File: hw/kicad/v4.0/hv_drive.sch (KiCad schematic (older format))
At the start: 21 parts, among them P6 CONN_01X02, P8 CONN_01X03, U12 IRAM256a

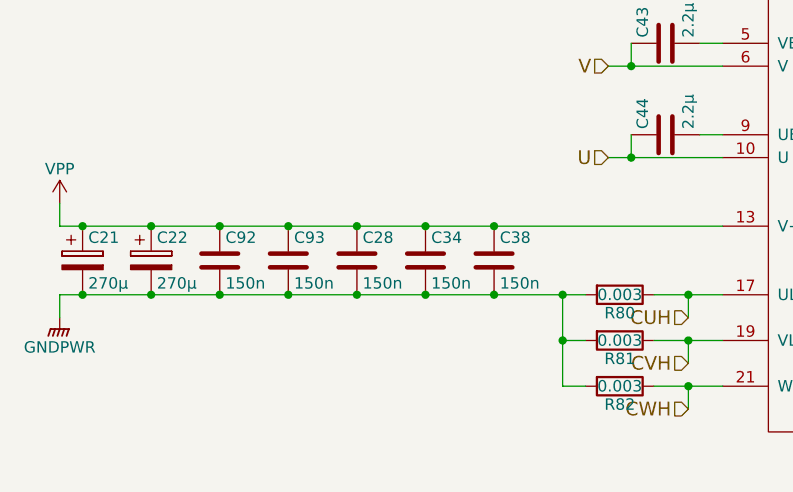
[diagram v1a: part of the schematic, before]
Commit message: Changed 120uf 1808 to 1210 100uF
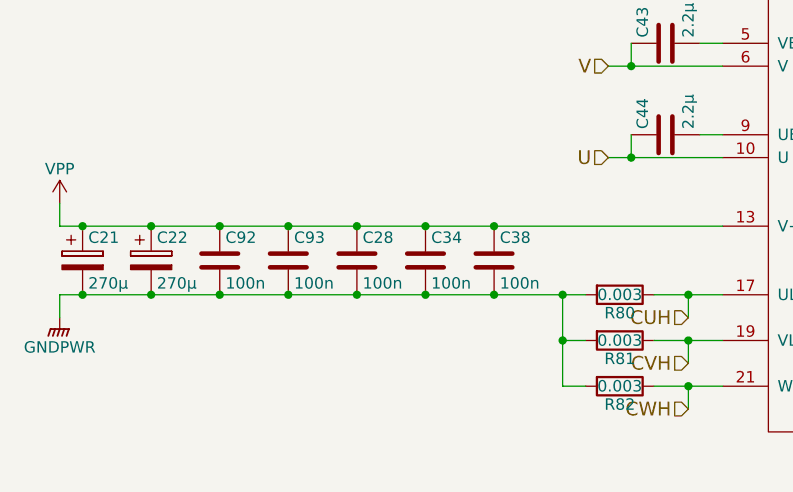
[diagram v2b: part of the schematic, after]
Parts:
- C14: LCSC C15850 -> C15850
- C147, C63: LCSC C14663 -> C14663
- C28, C34, C38, C92, C93: value 150n -> 100n; footprint stmbl:C_1808 -> Capacitor_SMD:C_1210_3225Metric; LCSC (none) -> C141218; Manufacturer No C1808W154KCRACTU -> C1210C104KCRAC7800
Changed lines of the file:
@@
 P 4250 4400
 F 0 "C28" H 4275 4500 50  0000 L CNN
-F 1 "150n" H 4275 4300 50  0000 L CNN
-F 2 "stmbl:C_1808" H 4288 4250 30  0001 C CNN
+F 1 "100n" H 4275 4300 50  0000 L CNN
+F 2 "Capacitor_SMD:C_1210_3225Metric" H 4288 4250 30  0001 C CNN
 F 3 "" H 4250 4400 60  0000 C CNN
 F 4 "" H 4250 4400 60  0001 C CNN "InternalName"
-F 5 "C1808W154KCRACTU" H 4250 4400 60  0001 C CNN "Manufacturer No"
+F 5 "C1210C104KCRAC7800" H 4250 4400 60  0001 C CNN "Manufacturer No"
 F 6 "500V" H 4250 4400 60  0001 C CNN "Voltage"
 F 7 "" H 4250 4400 60  0001 C CNN "Source"
@@
 F 9 "" H 0   0   50  0001 C CNN "Description"
 F 10 "KEMET" H 0   0   50  0001 C CNN "Manufacturer"
+F 11 "C141218" H 4250 4400 50  0001 C CNN "LCSC"
 	1    4250 4400
 	1    0    0    -1
@@
 P 4550 4400
 F 0 "C34" H 4575 4500 50  0000 L CNN
-F 1 "150n" H 4575 4300 50  0000 L CNN
-F 2 "stmbl:C_1808" H 4588 4250 30  0001 C CNN
+F 1 "100n" H 4575 4300 50  0000 L CNN
+F 2 "Capacitor_SMD:C_1210_3225Metric" H 4588 4250 30  0001 C CNN
 F 3 "" H 4550 4400 60  0000 C CNN
 F 4 "" H 4550 4400 60  0001 C CNN "InternalName"
-F 5 "C1808W154KCRACTU" H 4550 4400 60  0001 C CNN "Manufacturer No"
+F 5 "C1210C104KCRAC7800" H 4550 4400 60  0001 C CNN "Manufacturer No"
 F 6 "500V" H 4550 4400 60  0001 C CNN "Voltage"
 F 7 "" H 4550 4400 60  0001 C CNN "Source"
@@
 F 9 "" H 0   0   50  0001 C CNN "Description"
 F 10 "KEMET" H 0   0   50  0001 C CNN "Manufacturer"
+F 11 "C141218" H 4550 4400 50  0001 C CNN "LCSC"
 	1    4550 4400
 	1    0    0    -1
@@
 F 9 "" H 0   0   50  0001 C CNN "Description"
 F 10 "" H 0   0   50  0001 C CNN "Manufacturer"
-F 11 " C14663" H 7800 4900 50  0001 C CNN "LCSC"
+F 11 "C14663" H 7800 4900 50  0001 C CNN "LCSC"
 	1    7800 4900
 	1    0    0    -1
@@
 P 4850 4400
 F 0 "C38" H 4875 4500 50  0000 L CNN
-F 1 "150n" H 4875 4300 50  0000 L CNN
-F 2 "stmbl:C_1808" H 4888 4250 30  0001 C CNN
+F 1 "100n" H 4875 4300 50  0000 L CNN
+F 2 "Capacitor_SMD:C_1210_3225Metric" H 4888 4250 30  0001 C CNN
 F 3 "" H 4850 4400 60  0000 C CNN
 F 4 "" H 4850 4400 60  0001 C CNN "InternalName"
-F 5 "C1808W154KCRACTU" H 4850 4400 60  0001 C CNN "Manufacturer No"
+F 5 "C1210C104KCRAC7800" H 4850 4400 60  0001 C CNN "Manufacturer No"
 F 6 "500V" H 4850 4400 60  0001 C CNN "Voltage"
 F 7 "" H 4850 4400 60  0001 C CNN "Source"
@@
 F 9 "" H 0   0   50  0001 C CNN "Description"
 F 10 "KEMET" H 0   0   50  0001 C CNN "Manufacturer"
+F 11 "C141218" H 4850 4400 50  0001 C CNN "LCSC"
 	1    4850 4400
 	1    0    0    -1
@@
 P 3950 4400
 F 0 "C93" H 3975 4500 50  0000 L CNN
-F 1 "150n" H 3975 4300 50  0000 L CNN
-F 2 "stmbl:C_1808" H 3988 4250 30  0001 C CNN
+F 1 "100n" H 3975 4300 50  0000 L CNN
+F 2 "Capacitor_SMD:C_1210_3225Metric" H 3988 4250 30  0001 C CNN
 F 3 "" H 3950 4400 60  0000 C CNN
 F 4 "" H 3950 4400 60  0001 C CNN "InternalName"
-F 5 "C1808W154KCRACTU" H 3950 4400 60  0001 C CNN "Manufacturer No"
+F 5 "C1210C104KCRAC7800" H 3950 4400 60  0001 C CNN "Manufacturer No"
 F 6 "500V" H 3950 4400 60  0001 C CNN "Voltage"
 F 7 "" H 3950 4400 60  0001 C CNN "Source"
@@
 F 9 "" H 0   0   50  0001 C CNN "Description"
 F 10 "KEMET" H 0   0   50  0001 C CNN "Manufacturer"
+F 11 "C141218" H 3950 4400 50  0001 C CNN "LCSC"
 	1    3950 4400
 	1    0    0    -1
@@
 P 3650 4400
 F 0 "C92" H 3675 4500 50  0000 L CNN
-F 1 "150n" H 3675 4300 50  0000 L CNN
-F 2 "stmbl:C_1808" H 3688 4250 30  0001 C CNN
+F 1 "100n" H 3675 4300 50  0000 L CNN
+F 2 "Capacitor_SMD:C_1210_3225Metric" H 3688 4250 30  0001 C CNN
 F 3 "" H 3650 4400 60  0000 C CNN
 F 4 "" H 3650 4400 60  0001 C CNN "InternalName"
-F 5 "C1808W154KCRACTU" H 3650 4400 60  0001 C CNN "Manufacturer No"
+F 5 "C1210C104KCRAC7800" H 3650 4400 60  0001 C CNN "Manufacturer No"
 F 6 "500V" H 3650 4400 60  0001 C CNN "Voltage"
 F 7 "" H 3650 4400 60  0001 C CNN "Source"
@@
 F 9 "" H 0   0   50  0001 C CNN "Description"
 F 10 "KEMET" H 0   0   50  0001 C CNN "Manufacturer"
+F 11 "C141218" H 3650 4400 50  0001 C CNN "LCSC"
 	1    3650 4400
 	1    0    0    -1
@@
 F 9 "" H 0   0   50  0001 C CNN "Description"
 F 10 "" H 0   0   50  0001 C CNN "Manufacturer"
-F 11 " C15850" H 8400 4900 50  0001 C CNN "LCSC"
+F 11 "C15850" H 8400 4900 50  0001 C CNN "LCSC"
 	1    8400 4900
 	1    0    0    1
@@
 F 9 "" H 0   0   50  0001 C CNN "Description"
 F 10 "" H 0   0   50  0001 C CNN "Manufacturer"
-F 11 " C14663" H 8800 4900 50  0001 C CNN "LCSC"
+F 11 "C14663" H 8800 4900 50  0001 C CNN "LCSC"
 	1    8800 4900
 	1    0    0    -1

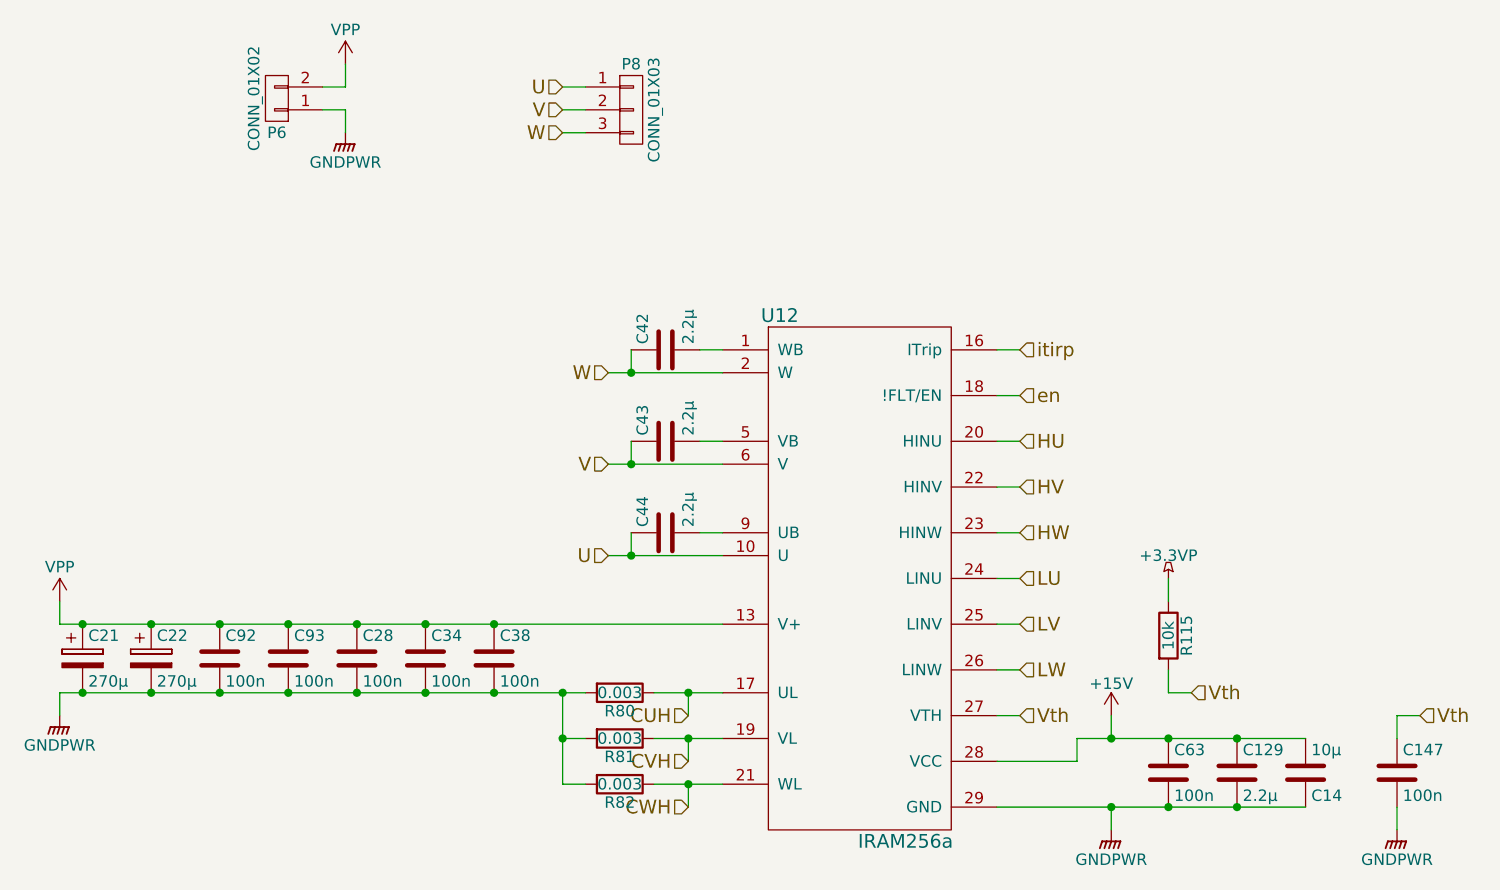
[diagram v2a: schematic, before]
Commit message: Switch some 2.2uf 0603 to 1uf bypass to get 50V version on jlcpcb
Change 2.2uf 0603 to 0805 on iram to get 50V version on jlcpcb
other cleanup
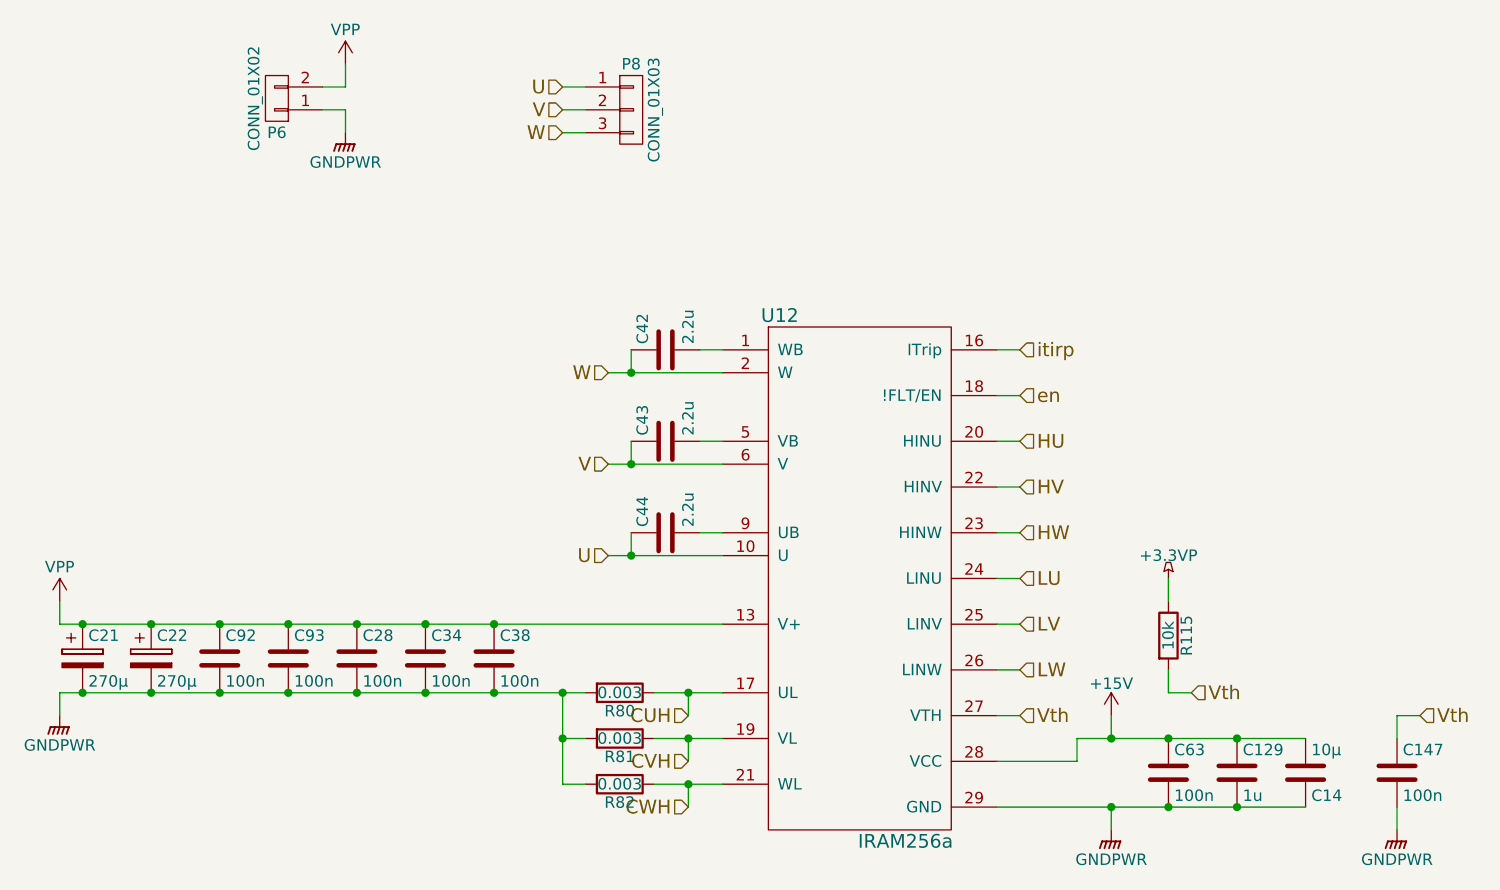
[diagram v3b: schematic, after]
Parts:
- C129: value 2.2µ -> 1u; LCSC C23630 -> C15849; Manufacturer (none) -> Samsung Electro-Mechanics; Manufacturer No (none) -> CL10A105KB8NNNC
- C14: Manufacturer (none) -> Samsung Electro-Mechanics; Manufacturer No (none) -> CL21A106KAYNNNE
- C147, C63: Manufacturer (none) -> YAGEO; Manufacturer No (none) -> CC0603KRX7R9BB104
- C42, C43, C44: value 2.2µ -> 2.2u; footprint stmbl:C_0603 -> stmbl:C_0805; LCSC C23630 -> C49217; Manufacturer (none) -> Guangdong Fenghua; Manufacturer No (none) -> 0805F225M500NT
- P6: LCSC C3697 -> (none)
- P8: LCSC C8377 -> (none)
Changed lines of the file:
@@
 P 5600 3050
 F 0 "C42" H 5625 3150 50  0000 L CNN
-F 1 "2.2µ" H 5625 2950 50  0000 L CNN
-F 2 "stmbl:C_0603" H 5638 2900 30  0001 C CNN
+F 1 "2.2u" H 5625 2950 50  0000 L CNN
+F 2 "stmbl:C_0805" H 5638 2900 30  0001 C CNN
 F 3 "" H 5600 3050 60  0000 C CNN
 F 4 "" H 5600 3050 60  0001 C CNN "InternalName"
-F 5 "" H 5600 3050 60  0001 C CNN "Manufacturer No"
+F 5 "0805F225M500NT" H 5600 3050 60  0001 C CNN "Manufacturer No"
 F 6 "35V" H 5600 3050 60  0001 C CNN "Voltage"
 F 7 "" H 5600 3050 60  0001 C CNN "Source"
 F 8 "X5R" H 5600 3050 60  0001 C CNN "Tolerance"
 F 9 "" H 0   0   50  0001 C CNN "Description"
-F 10 "" H 0   0   50  0001 C CNN "Manufacturer"
-F 11 "C23630" H 5600 3050 50  0001 C CNN "LCSC"
+F 10 "Guangdong Fenghua" H 0   0   50  0001 C CNN "Manufacturer"
+F 11 "C49217" H 5600 3050 50  0001 C CNN "LCSC"
 	1    5600 3050
 	0    -1   -1   0
@@
 P 5600 3450
 F 0 "C43" H 5625 3550 50  0000 L CNN
-F 1 "2.2µ" H 5625 3350 50  0000 L CNN
-F 2 "stmbl:C_0603" H 5638 3300 30  0001 C CNN
+F 1 "2.2u" H 5625 3350 50  0000 L CNN
+F 2 "stmbl:C_0805" H 5638 3300 30  0001 C CNN
 F 3 "" H 5600 3450 60  0000 C CNN
 F 4 "" H 5600 3450 60  0001 C CNN "InternalName"
-F 5 "" H 5600 3450 60  0001 C CNN "Manufacturer No"
+F 5 "0805F225M500NT" H 5600 3450 60  0001 C CNN "Manufacturer No"
 F 6 "35V" H 5600 3450 60  0001 C CNN "Voltage"
 F 7 "" H 5600 3450 60  0001 C CNN "Source"
 F 8 "X5R" H 5600 3450 60  0001 C CNN "Tolerance"
 F 9 "" H 0   0   50  0001 C CNN "Description"
-F 10 "" H 0   0   50  0001 C CNN "Manufacturer"
-F 11 "C23630" H 5600 3450 50  0001 C CNN "LCSC"
+F 10 "Guangdong Fenghua" H 0   0   50  0001 C CNN "Manufacturer"
+F 11 "C49217" H 5600 3450 50  0001 C CNN "LCSC"
 	1    5600 3450
 	0    -1   -1   0
@@
 P 5600 3850
 F 0 "C44" H 5625 3950 50  0000 L CNN
-F 1 "2.2µ" H 5625 3750 50  0000 L CNN
-F 2 "stmbl:C_0603" H 5638 3700 30  0001 C CNN
+F 1 "2.2u" H 5625 3750 50  0000 L CNN
+F 2 "stmbl:C_0805" H 5638 3700 30  0001 C CNN
 F 3 "" H 5600 3850 60  0000 C CNN
 F 4 "" H 5600 3850 60  0001 C CNN "InternalName"
-F 5 "" H 5600 3850 60  0001 C CNN "Manufacturer No"
+F 5 "0805F225M500NT" H 5600 3850 60  0001 C CNN "Manufacturer No"
 F 6 "35V" H 5600 3850 60  0001 C CNN "Voltage"
 F 7 "" H 5600 3850 60  0001 C CNN "Source"
 F 8 "X5R" H 5600 3850 60  0001 C CNN "Tolerance"
 F 9 "" H 0   0   50  0001 C CNN "Description"
-F 10 "" H 0   0   50  0001 C CNN "Manufacturer"
-F 11 "C23630" H 5600 3850 50  0001 C CNN "LCSC"
+F 10 "Guangdong Fenghua" H 0   0   50  0001 C CNN "Manufacturer"
+F 11 "C49217" H 5600 3850 50  0001 C CNN "LCSC"
 	1    5600 3850
 	0    -1   -1   0
@@
 F 3 "" H 7800 4900 60  0000 C CNN
 F 4 "" H 7800 4900 60  0001 C CNN "InternalName"
-F 5 "" H 7800 4900 60  0001 C CNN "Manufacturer No"
+F 5 "CC0603KRX7R9BB104 " H 7800 4900 60  0001 C CNN "Manufacturer No"
 F 6 "50V" H 7800 4900 60  0001 C CNN "Voltage"
 F 7 "" H 7800 4900 60  0001 C CNN "Source"
 F 8 "X5R" H 7800 4900 60  0001 C CNN "Tolerance"
 F 9 "" H 0   0   50  0001 C CNN "Description"
-F 10 "" H 0   0   50  0001 C CNN "Manufacturer"
+F 10 "YAGEO" H 0   0   50  0001 C CNN "Manufacturer"
 F 11 "C14663" H 7800 4900 50  0001 C CNN "LCSC"
 	1    7800 4900
@@
 F 9 "" H 0   0   50  0001 C CNN "Description"
 F 10 "Phoenix" H 0   0   50  0001 C CNN "Manufacturer"
-F 11 "C8377" H 5450 2000 50  0001 C CNN "LCSC"
+F 11 "" H 5450 2000 50  0001 C CNN "LCSC"
 	1    5450 2000
 	1    0    0    -1
@@
 F 9 "" H 0   0   50  0001 C CNN "Description"
 F 10 "Phoenix" H 0   0   50  0001 C CNN "Manufacturer"
-F 11 "C3697" H 3900 1950 50  0001 C CNN "LCSC"
+F 11 "" H 3900 1950 50  0001 C CNN "LCSC"
 	1    3900 1950
 	-1   0    0    1
@@
 P 8100 4900
 F 0 "C129" H 8125 5000 50  0000 L CNN
-F 1 "2.2µ" H 8125 4800 50  0000 L CNN
+F 1 "1u" H 8125 4800 50  0000 L CNN
 F 2 "stmbl:C_0603" H 8138 4750 30  0001 C CNN
 F 3 "" H 8100 4900 60  0000 C CNN
 F 4 "" H 8100 4900 60  0001 C CNN "InternalName"
-F 5 "" H 8100 4900 60  0001 C CNN "Manufacturer No"
+F 5 "CL10A105KB8NNNC" H 8100 4900 60  0001 C CNN "Manufacturer No"
 F 6 "35V" H 8100 4900 60  0001 C CNN "Voltage"
 F 7 "" H 8100 4900 60  0001 C CNN "Source"
 F 8 "X5R" H 8100 4900 60  0001 C CNN "Tolerance"
 F 9 "" H 0   0   50  0001 C CNN "Description"
-F 10 "" H 0   0   50  0001 C CNN "Manufacturer"
-F 11 "C23630" H 8100 4900 50  0001 C CNN "LCSC"
+F 10 "Samsung Electro-Mechanics" H 0   0   50  0001 C CNN "Manufacturer"
+F 11 "C15849" H 8100 4900 50  0001 C CNN "LCSC"
 	1    8100 4900
 	1    0    0    -1
@@
 F 4 "25V" H 8400 4900 60  0001 C CNN "Voltage"
 F 5 "" H 8400 4900 60  0001 C CNN "InternalName"
-F 6 "" H 8400 4900 60  0001 C CNN "Manufacturer No"
+F 6 "CL21A106KAYNNNE" H 8400 4900 60  0001 C CNN "Manufacturer No"
 F 7 "" H 8400 4900 60  0001 C CNN "Source"
 F 8 "X5R" H 8400 4900 60  0001 C CNN "Tolerance"
 F 9 "" H 0   0   50  0001 C CNN "Description"
-F 10 "" H 0   0   50  0001 C CNN "Manufacturer"
+F 10 "Samsung Electro-Mechanics" H 0   0   50  0001 C CNN "Manufacturer"
 F 11 "C15850" H 8400 4900 50  0001 C CNN "LCSC"
 	1    8400 4900
@@
 F 3 "" H 8800 4900 60  0000 C CNN
 F 4 "" H 8800 4900 60  0001 C CNN "InternalName"
-F 5 "" H 8800 4900 60  0001 C CNN "Manufacturer No"
+F 5 "CC0603KRX7R9BB104 " H 8800 4900 60  0001 C CNN "Manufacturer No"
 F 6 "50V" H 8800 4900 60  0001 C CNN "Voltage"
 F 7 "" H 8800 4900 60  0001 C CNN "Source"
 F 8 "X5R" H 8800 4900 60  0001 C CNN "Tolerance"
 F 9 "" H 0   0   50  0001 C CNN "Description"
-F 10 "" H 0   0   50  0001 C CNN "Manufacturer"
+F 10 "YAGEO" H 0   0   50  0001 C CNN "Manufacturer"
 F 11 "C14663" H 8800 4900 50  0001 C CNN "LCSC"
 	1    8800 4900
